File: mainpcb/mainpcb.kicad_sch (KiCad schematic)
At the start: 2 parts, among them J1 Raspberry_Pi_2_3, U1 PCA9615DP

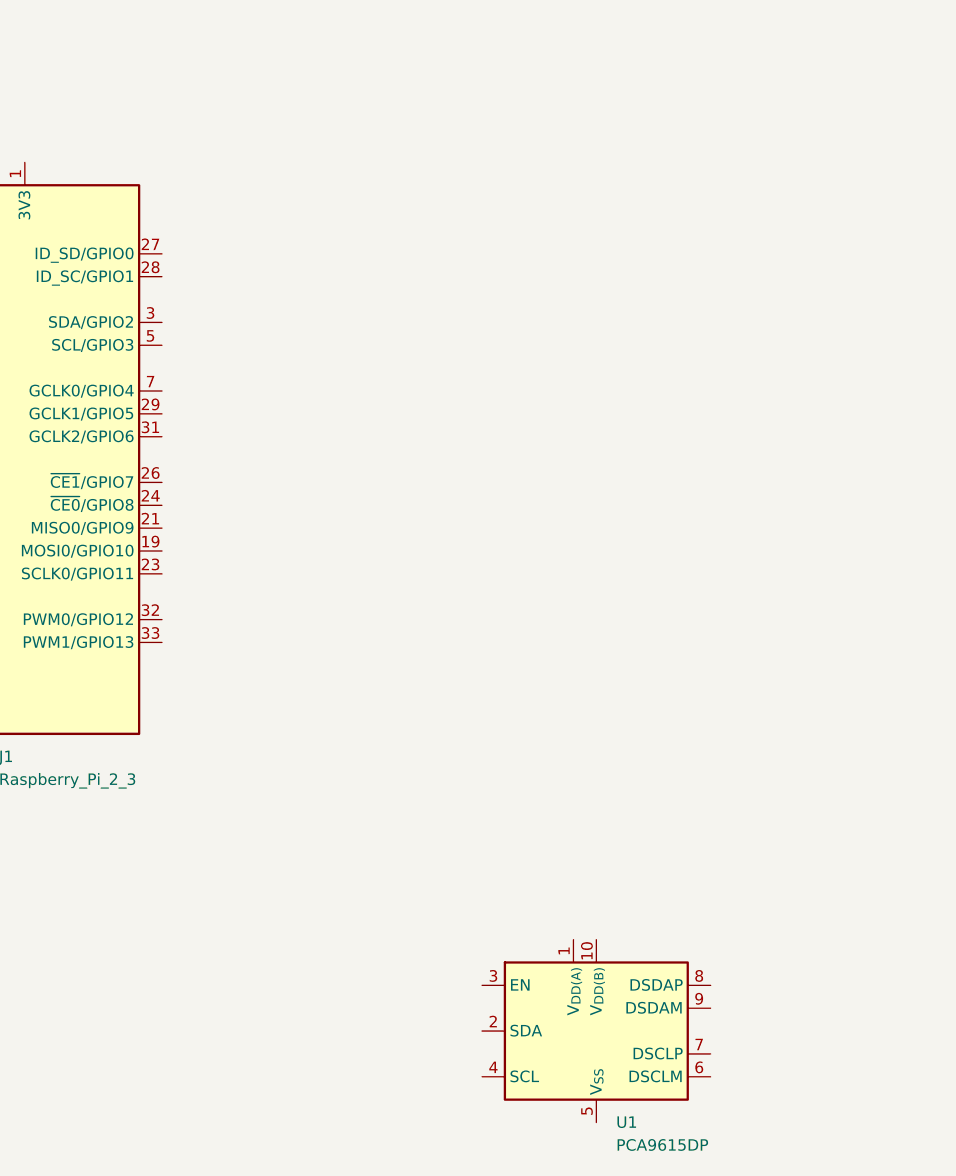
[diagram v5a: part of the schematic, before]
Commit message: Added TCA9517 I2C level shifter
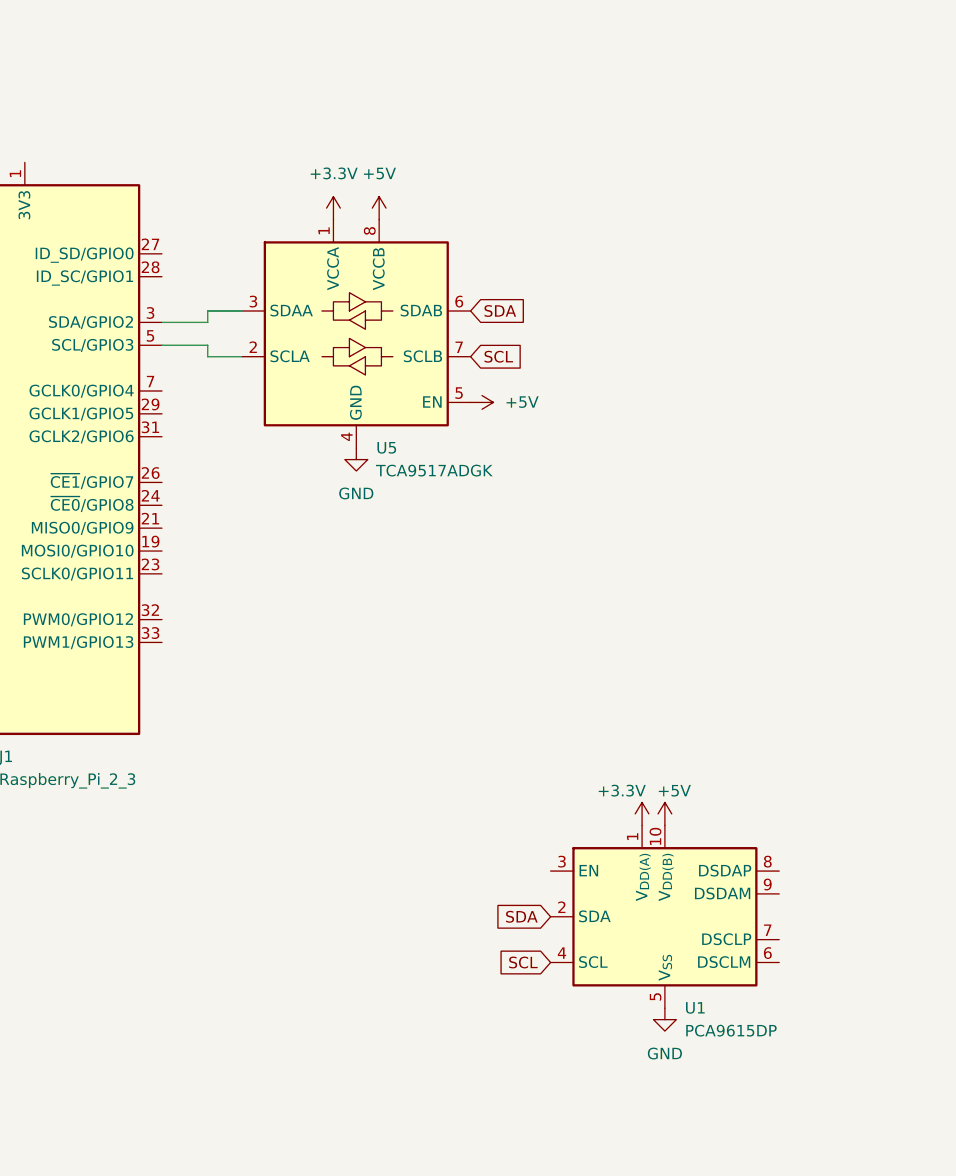
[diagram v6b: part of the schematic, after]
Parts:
- added U5: TCA9517ADGK, Package_SO:VSSOP-8_3x3mm_P0.65mm, symbol Logic_LevelTranslator:TCA9517ADGK
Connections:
- net +5V: now also U1.10 (V_{DD(B)}), U5.5 (EN), U5.8 (VCCB)
- net GND: now also U1.5 (V_{SS}), U5.4 (GND)
- net at J1.3 (SDA/GPIO2): now also U5.3 (SDAA)
- net at J1.5 (SCL/GPIO3): now also U5.2 (SCLA)
- net +3.3V: now reaches U1.1 (V_{DD(A)})
- net +3.3V: now also U5.1 (VCCA)
- net SDA: now reaches U1.2 (SDA)
- net SDA: now also U5.6 (SDAB)
- net SCL: now reaches U1.4 (SCL)
- net SCL: now also U5.7 (SCLB)
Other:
- moved on the sheet: U1

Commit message: I2C diff. and single side bus changes
Added differential termination on each end. Todo: determine maximum differential bias voltage. Added pull up resistors for I2C lines.

Added decoupling caps.
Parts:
- added C12: 0.1uF, Capacitor_THT:C_Disc_D8.0mm_W2.5mm_P5.00mm, symbol Device:C
- added J3: 8P8C_Shielded, Connector_RJ:RJ45_Amphenol_RJHSE5380, symbol Connector:8P8C_Shielded
- added R1, R3, R4, R6: 120R, symbol Device:R_US
- added R2, R5: 600R, symbol Device:R_US
- added R7, R8: 10kR, symbol Device:R_US
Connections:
- net +3.3V: now also J1.1 (3V3), J1.17 (3V3); no longer U1.1 (V_{DD(A)})
- net +5V: now also U1.1 (V_{DD(A)}), U1.3 (EN), C12.1, J3.5, R1.1, R4.1, R7.1, R8.2
- net GND: now also C12.2, J3.6, J3.8, J3.SH, R3.2, R6.2
- net SCL: now also R8.1
- net SDA: now also R7.2
- net DSCL-: now reaches U1.6 (DSCLM)
- net DSCL-: now also J3.1, R5.2, R6.1
- net DSCL+: now reaches U1.7 (DSCLP)
- net DSCL+: now also J3.2, R4.2, R5.1
- net DSDA+: now reaches U1.8 (DSDAP)
- net DSDA+: now also J3.4, R1.2, R2.1
- net DSDA-: now reaches U1.9 (DSDAM)
- net DSDA-: now also J3.3, R2.2, R3.1
- new net +12V: J3.7
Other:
- moved on the sheet: J1, U1, U5

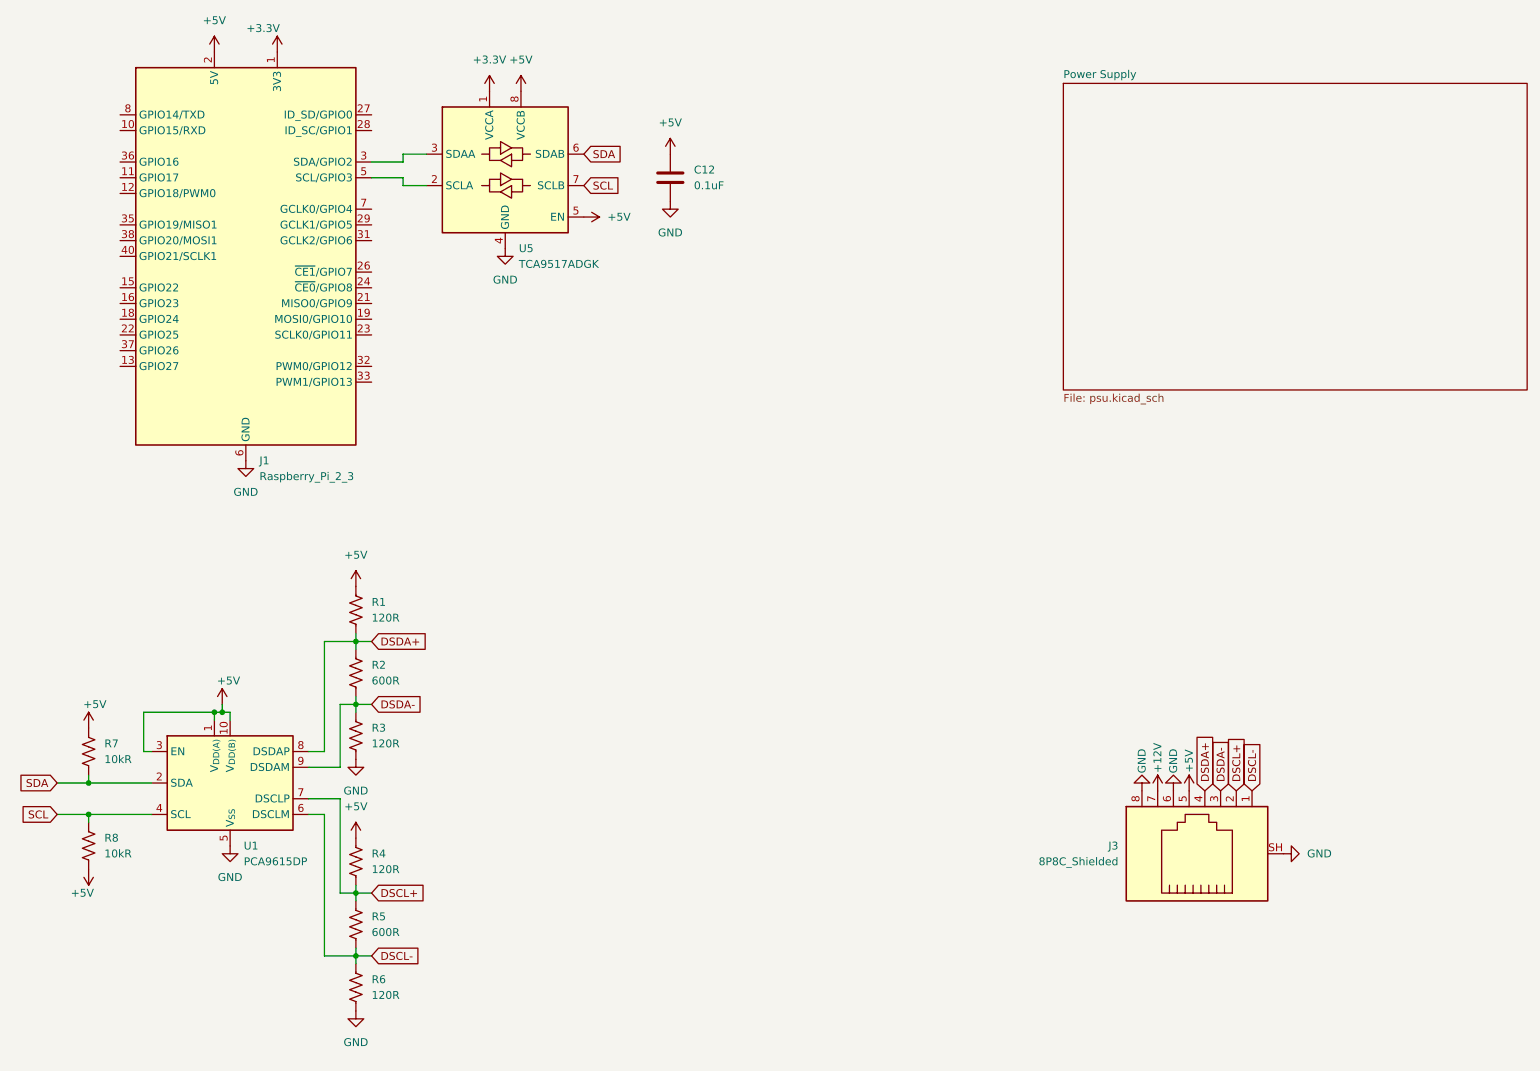
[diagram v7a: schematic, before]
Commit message: Added debug headers to stuff
Added debug headers to I2C single ended lines and differential lines
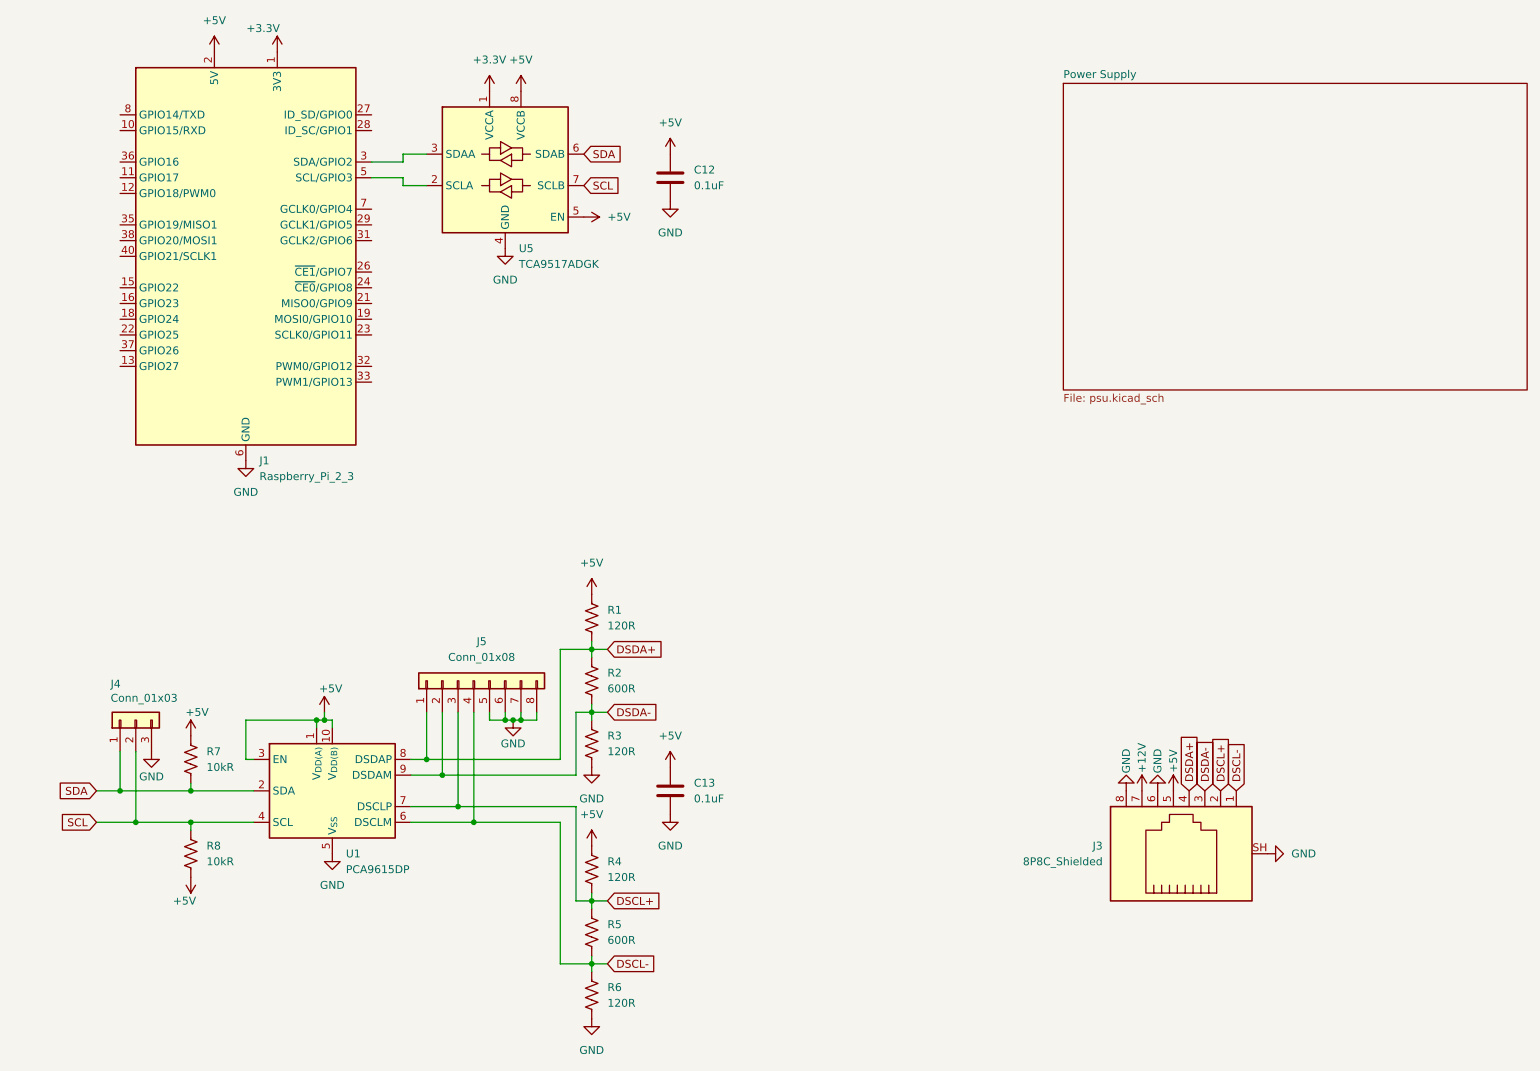
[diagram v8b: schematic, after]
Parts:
- added C13: 0.1uF, Capacitor_THT:C_Disc_D8.0mm_W2.5mm_P5.00mm, symbol Device:C
- added J4: Conn_01x03, Connector_PinHeader_2.54mm:PinHeader_1x03_P2.54mm_Vertical, symbol Connector_Generic:Conn_01x03
- added J5: Conn_01x08, Connector_PinHeader_2.54mm:PinHeader_1x08_P2.54mm_Vertical, symbol Connector_Generic:Conn_01x08
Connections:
- net +5V: now also C13.1
- net DSCL+: now also J5.3 (Pin_3)
- net DSCL-: now also J5.4 (Pin_4)
- net DSDA+: now also J5.1 (Pin_1)
- net DSDA-: now also J5.2 (Pin_2)
- net GND: now also C13.2, J4.3 (Pin_3), J5.5 (Pin_5), J5.6 (Pin_6), J5.7 (Pin_7), J5.8 (Pin_8)
- net SCL: now also J4.2 (Pin_2)
- net SDA: now also J4.1 (Pin_1)
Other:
- moved on the sheet: J3, R1, R2, R3, R4, R5, R6, R7, R8, U1
